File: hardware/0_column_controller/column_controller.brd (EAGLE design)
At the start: 35.6 x 76.2 mm, 60 parts, among them J3 RJ45, J4 JTAG, J5 JTAG, J7 RJ45, U1 PCA9615

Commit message: remove 5V from AREF pin
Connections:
- net 5V: no longer U$13.AREF
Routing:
- net 5V: track 167.7 -> 159.0 mm
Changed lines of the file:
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@@
 <contactref element="C10" pad="1"/>
 <contactref element="U$13" pad="VIN"/>
-<contactref element="U$13" pad="AREF"/>
 <contactref element="J3" pad="3"/>
 <contactref element="J7" pad="3"/>
@@
 <via x="15.24" y="27.051" extent="1-16" drill="0.3"/>
 <wire x1="15.24" y1="27.051" x2="15.24" y2="28.36" width="0.6096" layer="1"/>
-<wire x1="22.86" y1="72.39" x2="21.59" y2="72.39" width="0.6096" layer="16"/>
-<wire x1="20.32" y1="71.12" x2="21.59" y2="72.39" width="0.6096" layer="16"/>
-<wire x1="22.86" y1="67.31" x2="21.59" y2="67.31" width="0.6096" layer="16"/>
-<wire x1="21.59" y1="67.31" x2="20.32" y2="68.58" width="0.6096" layer="16"/>
-<wire x1="20.32" y1="68.58" x2="20.32" y2="71.12" width="0.6096" layer="16"/>
 <wire x1="9.525" y1="27.051" x2="8.636" y2="26.162" width="0.6096" layer="16"/>
 <wire x1="8.636" y1="26.162" x2="8.636" y2="18.415" width="0.6096" layer="16"/>

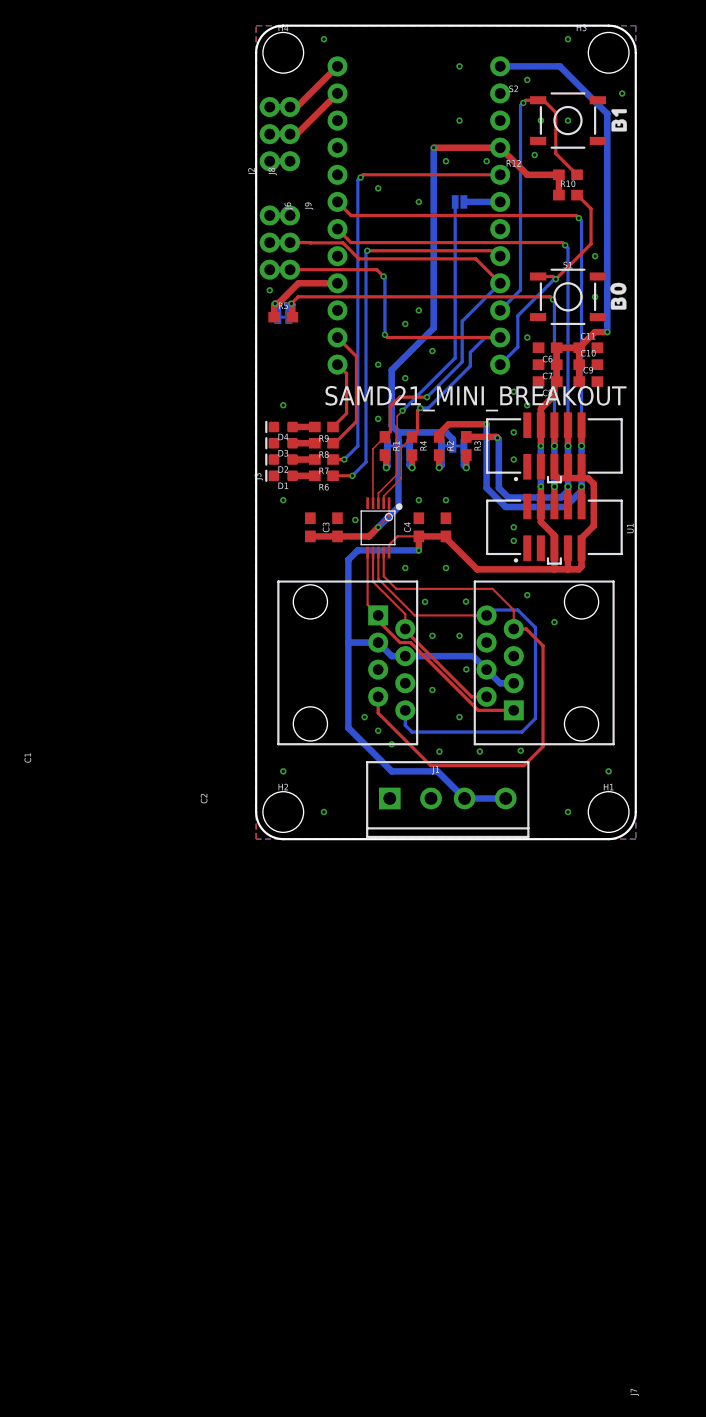
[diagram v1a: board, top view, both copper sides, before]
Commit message: change column controller back to esp32 w/ more leds
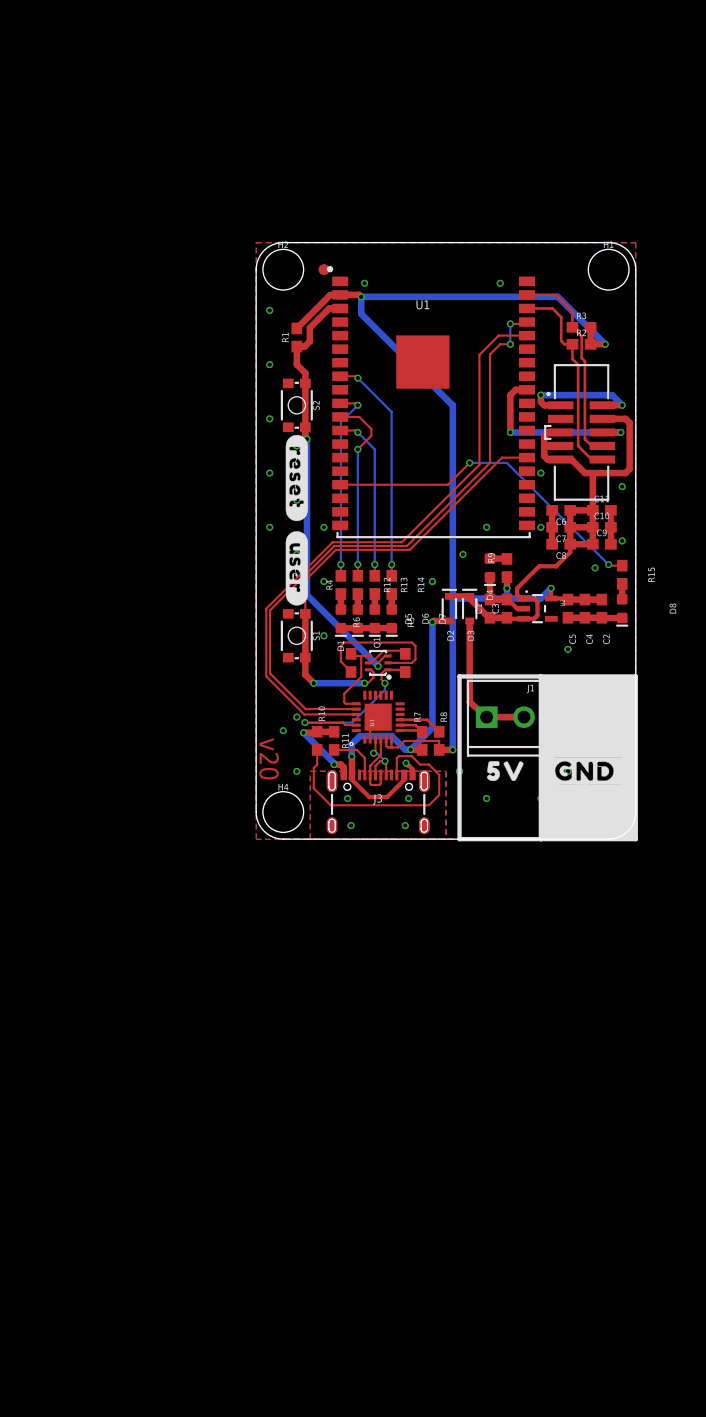
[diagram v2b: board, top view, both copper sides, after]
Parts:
- removed J2, J6, J8, J9: (no value), SparkFun-Connectors:1X03_NO_SILK
- removed J5: JTAG, SparkFun-Connectors:2X5-SMD-1.27MM
- removed J7: RJ45, SparkFun-Connectors:RJ45-8
- removed JP1: JUMPER-SMT_2_NC_TRACE_SILK, SparkFun-Jumpers:SMT-JUMPER_2_NC_TRACE_SILK
- removed JP2, JP3: JUMPER-SMT_3_2-NC_TRACE_SILK, SparkFun-Jumpers:SMT-JUMPER_3_2-NC_TRACE_SILK
- removed JP4: JUMPER-SMT_2_NO_SILK, SparkFun-Jumpers:SMT-JUMPER_2_NO_SILK
- removed U$13: SAMD21_MINI_BREAKOUT, SparkFun-Boards:SAMD21_MINI_BREAKOUT
- removed U$14: (no value), buzzard_labels:RXI5
- removed U$3: (no value), buzzard_labels:B11
- added C5: 4.7uF, SparkFun-Capacitors:0603
- added D5, D6, D7, D8: (no value), SparkFun-LED:LED-0603
- added FD1, FD2, FD3, FD4: FIDUCIAL1X2, SparkFun-Aesthetics:FIDUCIAL-1X2
- added Q1: (no value), SparkFun-DiscreteSemi:SC70-6
- added R11: 5.1k, SparkFun-Resistors:0603
- added R13, R14, R15: 1k, SparkFun-Resistors:0603
- added U2: 3.3V, SparkFun-IC-Power:SOT23-5
- added U3: CP2102N, SparkFun-IC-Comms:QFN24
- D1, D4: value BLUE -> (none)
- D2, D3: value BLUE -> 3A/10V/280mV; device SparkFun-LED:LED-0603 -> SparkFun-DiscreteSemi:SOD-323
- J1: device SparkFun-Connectors:SCREWTERMINAL-3.5MM-4_LOCK -> SparkFun-Connectors:SCREWTERMINAL-3.5MM-4
- J3: value RJ45 -> (none); device SparkFun-Connectors:RJ45-8 -> SparkFun-Connectors:USB-C-16P
- R1, R6: value 1k -> 10k
- R10: value 1k -> 5.1k
- R5: value DNP -> 10k
- R7: value 1k -> 10
- S1, S2: value MOMENTARY-SWITCH-SPST-SMD-5.2MM-TALL -> (none); device SparkFun-Switches:TACTILE_SWITCH_SMD_5.2MM -> SparkFun-Switches:TACTILE_SWITCH_SMD_4.6X2.8MM
- U$1: device buzzard_labels:OCLYKE#DEV7 -> buzzard_labels:5V2
- U$10: device buzzard_labels:NETWORK_SDA7 -> buzzard_labels:SUMMER_202010
- U$11: device buzzard_labels:NETWORK_SCL6 -> buzzard_labels:#PLAYZEUM#10
- U$12: device buzzard_labels:TXO4 -> SparkFun-Aesthetics:OSHW-LOGO-M
- U$2: device buzzard_labels:B00 -> buzzard_labels:#GND#6
- U$4: device buzzard_labels:5V2 -> buzzard_labels:#USER#2
- U$5: device buzzard_labels:#GND#6 -> buzzard_labels:#RESET#3
- U$6: device buzzard_labels:PCA_EN2 -> ocl_L#PNG:OCL_L#PNG
- U$7: device buzzard_labels:DOUT_BYP3 -> buzzard_labels:MUSEUM_OF_BOULDER9
- U$8: device buzzard_labels:COLUMN_I2C4 -> buzzard_labels:OCLYKE#DEV7
- U$9: device buzzard_labels:NETWORK_I2C4 -> buzzard_labels:#RAINBOW_FOREST#8
- U1: value PCA9615 -> ESP-WROVER-32ESP-WROVER-32; device SparkFun-IC-Comms:TSSOP10 -> SparkFun-RF:ESP-WROVER-32
- moved H3 71.1 mm to (33.0, 2.54)
- moved H4 71.1 mm to (2.54, 2.54)
- moved U$12 66.2 mm to (17.8, 2.54)
- moved R10 56.3 mm to (5.71, 9.21), turned to 270 degrees
- moved H1 50.8 mm to (33.0, 53.3)
- moved H2 50.8 mm to (2.54, 53.3)
- moved U$11 49.8 mm to (35.9, 8.64)
- moved U$10 45.0 mm to (16.0, 8.51)
- moved U$7 44.2 mm to (36.8, 11.4), turned to 0 degrees
- moved R12 43.2 mm to (9.53, 23.8), turned to 90 degrees
- moved U$2 42.8 mm to (26.7, 6.35), turned to 0 degrees
- moved S1 40.7 mm to (3.81, 19.1), turned to 270 degrees
- moved U$5 39.4 mm to (3.81, 37.8), flipped to the top, turned to 270 degrees
- moved S2 36.8 mm to (3.81, 40.6), turned to 270 degrees
- moved R5 34.3 mm to (14.0, 16.5), turned to 270 degrees
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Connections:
- removed net B0: R10.2, S1.1, U$13.PA18
- removed net B1: R12.2, S2.1, U$13.PA19
- removed net DSCL_N: J3.1, J7.1, U1.6
- removed net DSCL_P: J3.2, J7.2, U1.7
- removed net DSDA_N: J3.7, J7.7, U1.9
- removed net DSDA_P: J3.8, J7.8, U1.8
- removed net LED0: R6.1, U$13.PA02
- removed net LED1: R7.1, U$13.PA04
- removed net LED2: R8.1, U$13.PA06
- removed net LED3: R9.1, U$13.PA07
- removed net PCA_EN: JP4.2, U1.3
- removed net RXI: J2.2, J8.2, U$13.PA11
- removed net SCL_COLUMN: J4.10, J5.10, R2.1, U$13.PA09
- removed net SCL_NETWORK: J6.2, J9.2, R1.1, U$13.PA17, U1.4
- removed net SDA_COLUMN: J4.8, J5.8, R3.1, U$13.PA08
- removed net SDA_NETWORK: J6.3, J9.3, R4.1, U$13.PA16, U1.2
- removed net TXO: J2.3, J8.3, U$13.PA10
- new net !RESET: Q1.3, R1.1, S2.3, S2.4, U1.P$3
- new net 0: Q1.6, S1.3, S1.4, U1.P$25
- new net 13: R15.2, U1.P$16
- new net 25: R4.2, U1.P$10
- new net 26: R12.2, U1.P$11
- new net 27: R13.2, U1.P$12
- new net 32: R14.2, U1.P$8
- new net DTR: Q1.1, R5.2, U3.23
- new net N$11: J3.B5, R10.2
- new net N$12: D6.A, R13.1
- new net N$13: D7.A, R14.1
- new net N$14: D8.A, R15.1
- new net RTS: Q1.4, R6.2, U3.19
- new net RX: U1.P$35, U3.20
- new net SCL: J4.10, R2.1, U1.P$36
- new net SDA: J4.8, R3.1, U1.P$37
- new net SHLD: J3.SHLD1, J3.SHLD2, J3.SHLD3, J3.SHLD4, J3.SHLD5, J3.SHLD6, J3.SHLD7, J3.SHLD8
- new net TX: U1.P$34, U3.21
- new net VIN: D3.A, J1.1, J1.2
- new net V_USB: D2.A, J3.VBUS1, J3.VBUS2, R7.1
- net 3.3V: now also C2.1, C4.1, C5.1, R1.2, R2.2, R3.2, R8.2, R9.2, U1.P$2, U2.5, U3.5, U3.6; no longer C1.1, C3.1, JP2.2, JP3.2, R10.1, R12.1, U$13.3V3, U1.1
- net 5V: now also C1.1, C3.1, D2.C, D3.C, U2.1, U2.3; no longer C2.1, C4.1, J1.3, J1.4, J3.3, J3.4, J5.4, J5.5, J5.7, J5.9, J7.3, J7.4, U$13.VIN, U1.10
- net DOUT: now also U1.P$30; no longer J5.6, JP1.2, R5.2
- net GND: now also C5.2, D5.C, D6.C, D7.C, D8.C, J1.3, J1.4, J3.GND, J3.GND2, R10.1, R11.1, S1.1, S1.2, S2.1, S2.2, U1.P$1, U1.P$15, U1.P$38, U1.P$39, U2.2, U3.2, U3.PAD; no longer D2.C, D3.C, J1.1, J1.2, J2.1, J3.5, J3.6, J5.1, J5.2, J5.3, J6.1, J7.5, J7.6, J8.1, J9.1, S1.3, S2.3, U$13.GND, U$13.GND1, U1.5
- net N$1: now also J3.A7, J3.B7, U3.4; no longer JP1.1, R5.1, U$13.PA20
- net N$10: now also J3.A5, R11.2; no longer JP4.1, U$13.PB09
- net N$2: now also J3.A6, J3.B6, U3.3; no longer JP2.3, R1.2
- net N$3: now also Q1.2, R6.1; no longer JP2.1, R4.2
- net N$4: now also D1.A, R4.1; no longer JP3.3, R2.2
- net N$5: now also Q1.5, R5.1; no longer JP3.1, R3.2
- net N$6: now also R7.2, U3.7, U3.8; no longer D1.A, R6.2
- net N$7: now also R8.1, U3.9; no longer D4.A, R9.2
- net N$8: now also D4.A, R9.1; no longer D3.A, R8.2
- net N$9: now also D5.A, R12.1; no longer D2.A, R7.2
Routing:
- net 5V: track 159.0 -> 57.7 mm, vias 4 -> 0
- net SCL_COLUMN: track 74.0 -> 0.00 mm, vias 4 -> 0
- net SDA_COLUMN: track 63.7 -> 0.00 mm, vias 4 -> 0
- net RX: track 0.00 -> 57.7 mm, vias 0 -> 2
- net TX: track 0.00 -> 57.3 mm
- net SCL_NETWORK: track 50.2 -> 0.00 mm, vias 1 -> 0
- net DSDA_N: track 50.1 -> 0.00 mm
- net SDA_NETWORK: track 48.7 -> 0.00 mm, vias 3 -> 0
- net GND: track 3.81 -> 46.8 mm, vias 55 -> 35
- net DSDA_P: track 42.4 -> 0.00 mm
- net 0: track 0.00 -> 42.4 mm, vias 0 -> 2
- net LED1: track 41.3 -> 0.00 mm, vias 2 -> 0
- net !RESET: track 0.00 -> 41.2 mm, vias 0 -> 2
- net 3.3V: track 68.3 -> 107.2 mm, vias 2 -> 5
- net LED0: track 36.2 -> 0.00 mm, vias 2 -> 0
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- added copper zone on layer 1, net SHLD
- added copper zone on layer 16, net SHLD
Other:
- board size 35.6 x 76.2 mm -> 35.6 x 55.9 mm
- board text added: "v20"
- board text removed: "oclyke"
